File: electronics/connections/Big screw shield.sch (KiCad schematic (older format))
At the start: 0 parts

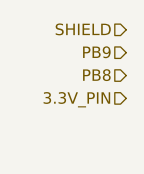
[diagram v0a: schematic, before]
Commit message: Add chain guide models
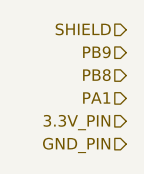
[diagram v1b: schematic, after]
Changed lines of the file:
@@
 $Descr A4 11693 8268
 encoding utf-8
-Sheet 19 20
+Sheet 18 22
 Title ""
 Date ""
@@
 Text HLabel 5700 4150 0    50   Input ~ 0
 PB8
+Text HLabel 5700 4350 0    50   Input ~ 0
+3.3V_PIN
+Text HLabel 5700 4450 0    50   Input ~ 0
+GND_PIN
 Text HLabel 5700 4250 0    50   Input ~ 0
-3.3V_PIN
+PA1
 $EndSCHEMATC

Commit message: Change connections
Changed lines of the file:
@@
 GND_PIN
 Text HLabel 5700 4250 0    50   Input ~ 0
-PA1
+PC0
 $EndSCHEMATC
